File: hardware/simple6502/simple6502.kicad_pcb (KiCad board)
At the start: 2 copper layers, 87 x 85.6 mm, 24 parts, among them J1 ~{VP}, J2 CLK SEL, J6 AUX 5VDC, U1 W65C02SxP, U2 RAM 62256, U3 ROM 28C256, U4 74LS30, U5 74HCT00, U6 74HC138, X1 ACO-1MHz

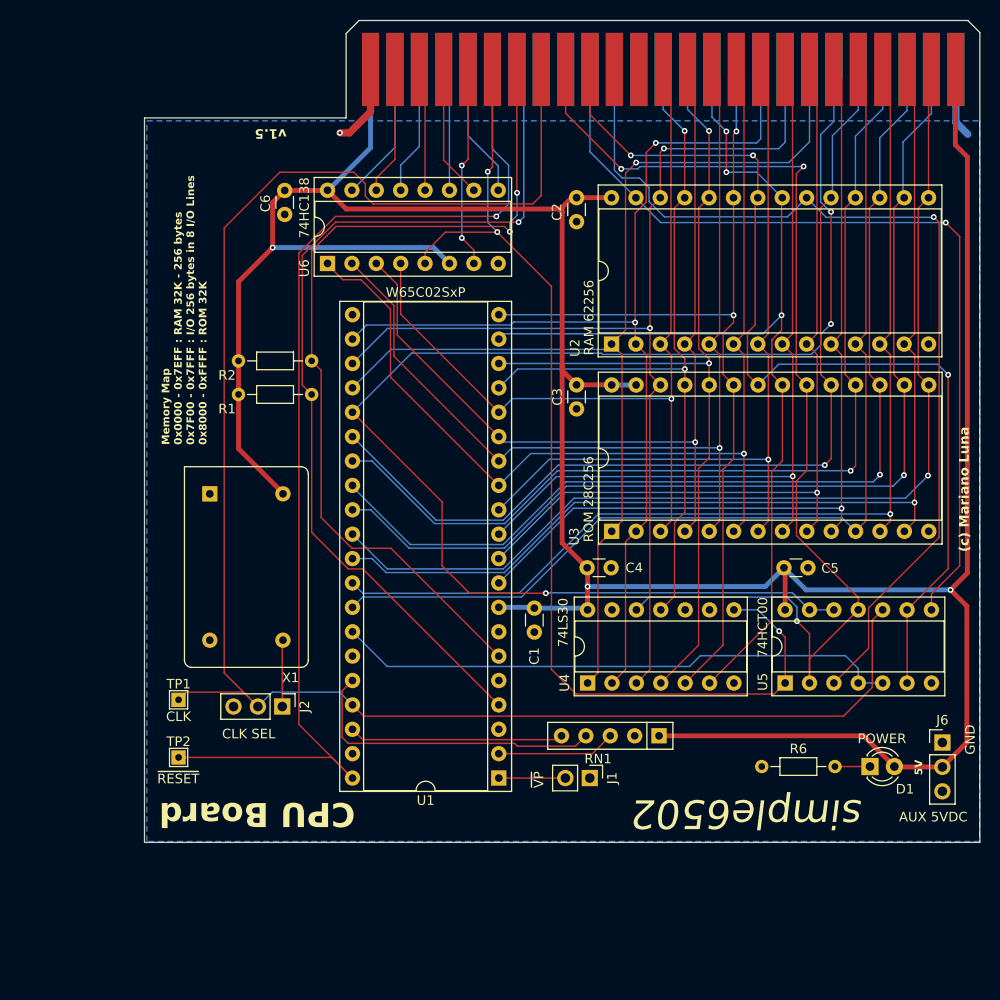
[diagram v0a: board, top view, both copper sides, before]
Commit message: Schematic and PCB cleanup
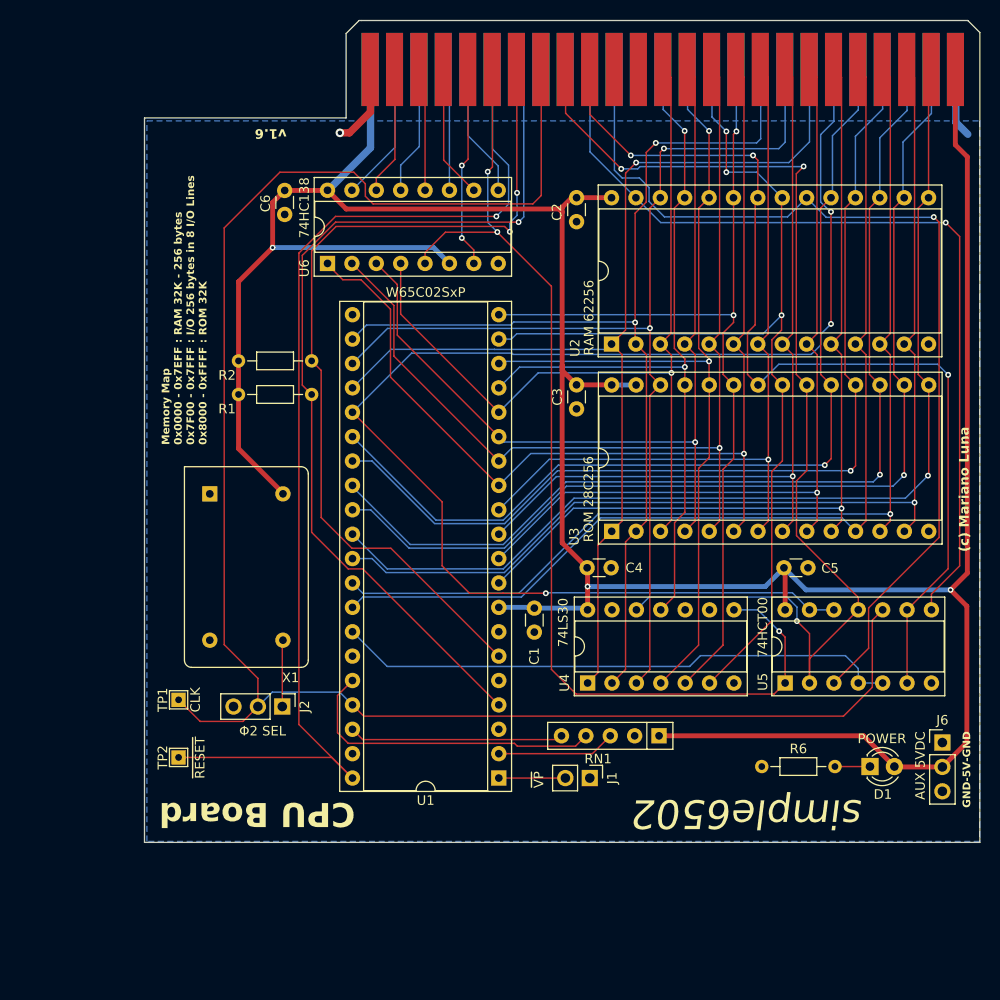
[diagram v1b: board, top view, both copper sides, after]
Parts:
- removed BUS1: 6502 BUS, Connector_PCBEdge:BUS_EdgePCB_Apple_2
- added SLOT1: 6502 BUS, Connector_PCBEdge:BUS_EdgePCB_Apple_2, F.Cu at (124.6, 55.1)
- J2: value CLK SEL -> Φ2 SEL
- turned TP1 to 90 degrees
- turned TP2 to 90 degrees
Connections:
- J2 pad 3: GND -> unconnected-(J2-Pin_3-Pad3)
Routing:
- net A7: track 88.2 -> 89.3 mm
- net CLK: track 187.0 -> 187.6 mm
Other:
- board text added: "GND-5V-GND"
- board text added: "Memory Map: 0x0000 - 0x7EFF : RAM 32K - 256 bytes 0x7F00 - 0x7FFF : I/O 256 bytes in 8 I/O Lines 0x8000 - 0xFFFF : ROM 32K"
- board text added: "v1.6"
- board text removed: "5V"
- board text removed: "GND"
- board text removed: "v1.5"

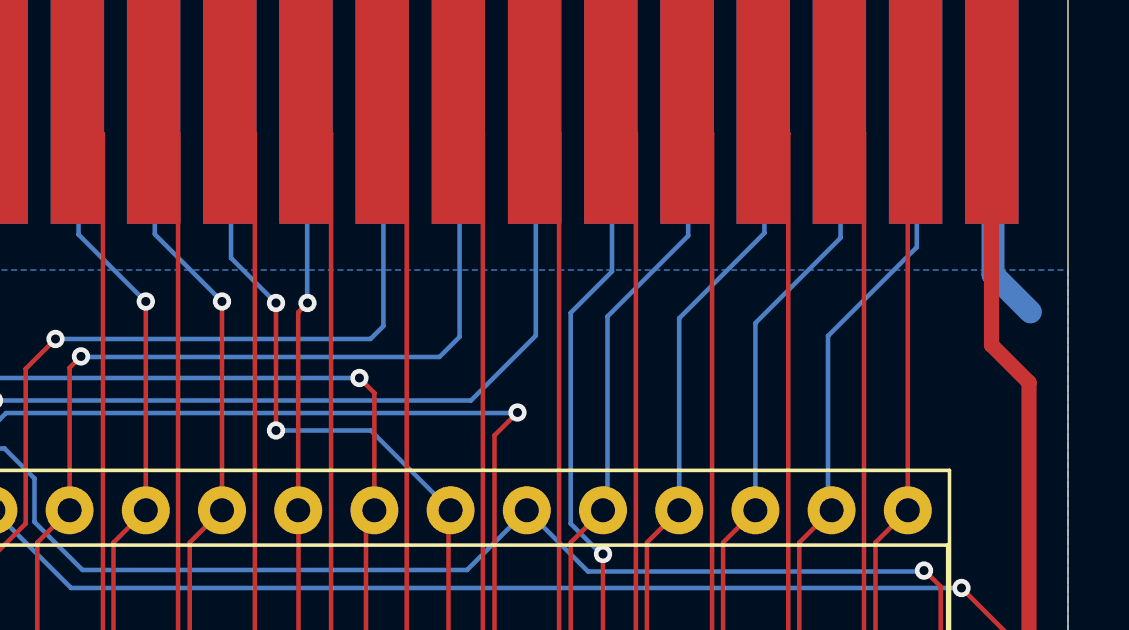
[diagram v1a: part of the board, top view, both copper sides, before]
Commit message: rev 1.8 new pcb optimized power routing
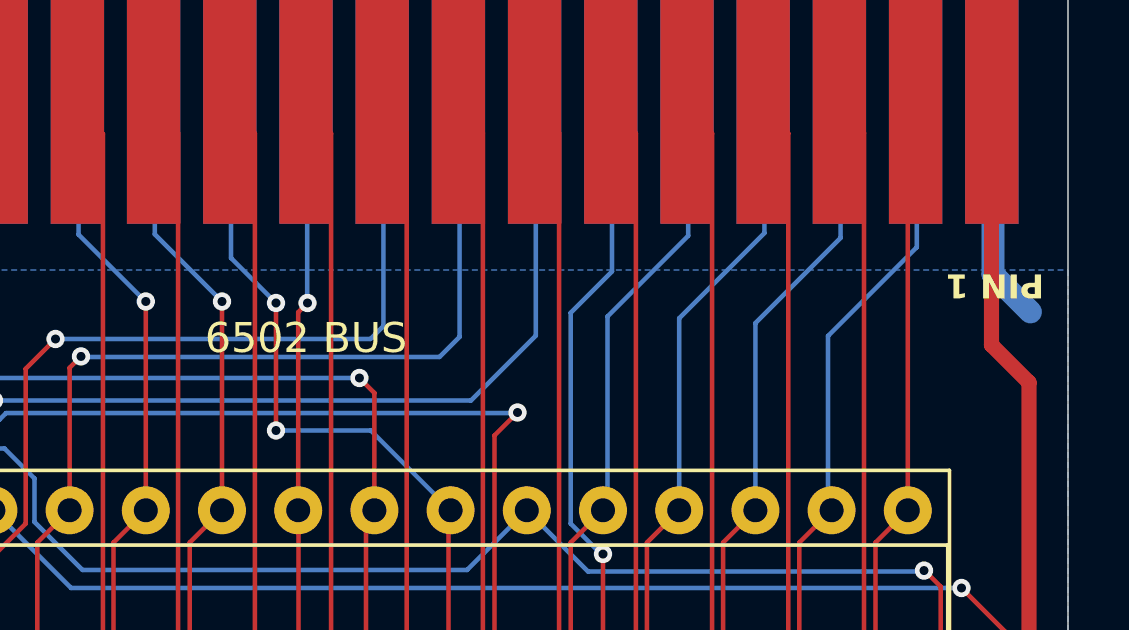
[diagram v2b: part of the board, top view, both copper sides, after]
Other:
- board text added: "PIN 1"
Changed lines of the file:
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@@
         (effects (font (size 1 1) (thickness 0.15)))
     )
-    (fp_text value "6502 BUS " (at 0 -7.62) (layer "F.Fab")
+    (fp_text value "6502 BUS " (at 0 -7.62 180) (layer "F.SilkS")
         (effects (font (size 1 1) (thickness 0.15)))
     )
@@
     (effects (font (size 1 1) (thickness 0.2) bold) (justify left bottom))
   )
+  (gr_text "PIN 1" (at 149.2 60.5 180) (layer "F.SilkS")
+    (effects (font (size 0.8 0.8) (thickness 0.15) bold) (justify left bottom))
+  )
   (gr_text "100x100mm PCBWay " (at 50 45) (layer "Cmts.User")

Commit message: Schematic rev 1.6 complete
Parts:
- moved J1 8.09 mm to (102.4, 133.0)
- moved X1 1.80 mm to (68.0, 99.2)
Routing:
- net /~{VP}: track 6.93 -> 4.12 mm
- net VCC: track 316.3 -> 315.5 mm
- net /OSC_OUT: track 6.94 -> 7.73 mm
- net A4: track 108.3 -> 107.6 mm

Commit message: cleanup and minor changes
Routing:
- net CLK: track 187.6 -> 175.4 mm
- net VCC: vias 3 -> 4
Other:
- board text added: "FRONT"
- board text added: "v${REVISION}"
- board text removed: "v1.6"

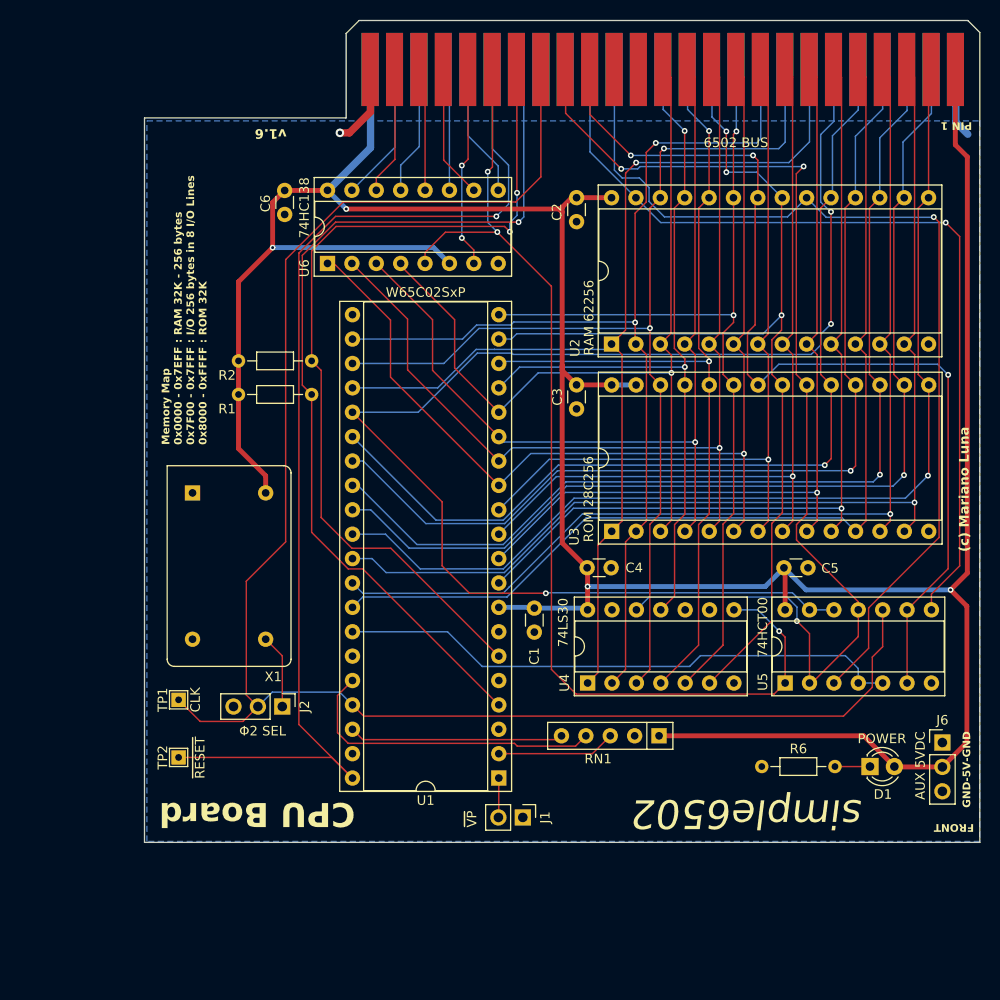
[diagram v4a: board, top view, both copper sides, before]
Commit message: Squashed commit of the following:
commit 7c3efda86e123a872d37b7a0967bfebff1f0e87c
Author: Mariano Luna <marianolu@gmail.com>
Date:   Wed Jun 26 21:29:25 2024 -0500

    added license to the read me

commit 04e24ff3751ecfd7aa1644195e6f678569023e69
Author: Mariano Luna <marianolu@gmail.com>
Date:   Wed Jun 26 21:19:54 2024 -0500

    typo fix for {\textunderscore}

commit 2b909ce419fda75b2b3b71af0dca9a0f271ced5f
Author: Mariano Luna <marianolu@gmail.com>
Date:   Wed Jun 26 21:10:17 2024 -0500

    updated ReadME and memory map in the schematic

commit 245ee8cf40a99742bf88408506d7aad409daa5ea
Author: Mariano Luna <marianolu@gmail.com>
Date:   Wed Jun 26 20:32:31 2024 -0500

    minor slikscreen additions

commit ba4f0f790206ee10e8f2da3f956f1fdfcce2d174
Author: Mariano Luna <marianolu@gmail.com>
Date:   Wed Jun 26 20:23:09 2024 -0500

    new PCB pics

commit 7135a14f7811bac113619ea70f1b15383090e088
Author: Mariano Luna <marianolu@gmail.com>
Date:   Wed Jun 26 20:16:23 2024 -0500

    minor silkscreen and trace tidy up

commit cb74d108b563011aa3ae8e77489211a7feb419d9
Author: Mariano Luna <marianolu@gmail.com>
Date:   Wed Jun 26 19:48:35 2024 -0500

    renumer components based on PCB placement

commit 755f9fae4396755bcef755a3da40c138a841726b
Author: Mariano Luna <marianolu@gmail.com>
Date:   Wed Jun 26 19:46:30 2024 -0500

    minor route changes

commit 2a8145687e928c766354ef12103bfb997fda5951
Author: Mariano Luna <marianolu@gmail.com>
Date:   Wed Jun 26 13:28:37 2024 -0500

    port wired, new slot pinout

commit 79f2ca33b26e56ed7b5b5aa909bf5c4120f9fd97
Author: Mariano Luna <marianolu@gmail.com>
Date:   Sat Jun 15 11:24:34 2024 -0500

    add the 40 pin header

commit 10816cce1296760c190b10fc9481db229a365134
Author: Mariano Luna <marianolu@gmail.com>
Date:   Tue Mar 26 20:31:24 2024 -0500

    Updated VCC routing

commit 6f1e481cf970100d714ca12a9d653bae0b6e1127
Author: Mariano Luna <marianolu@gmail.com>
Date:   Tue Mar 26 19:53:34 2024 -0500

    PCB ready DRC passed
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
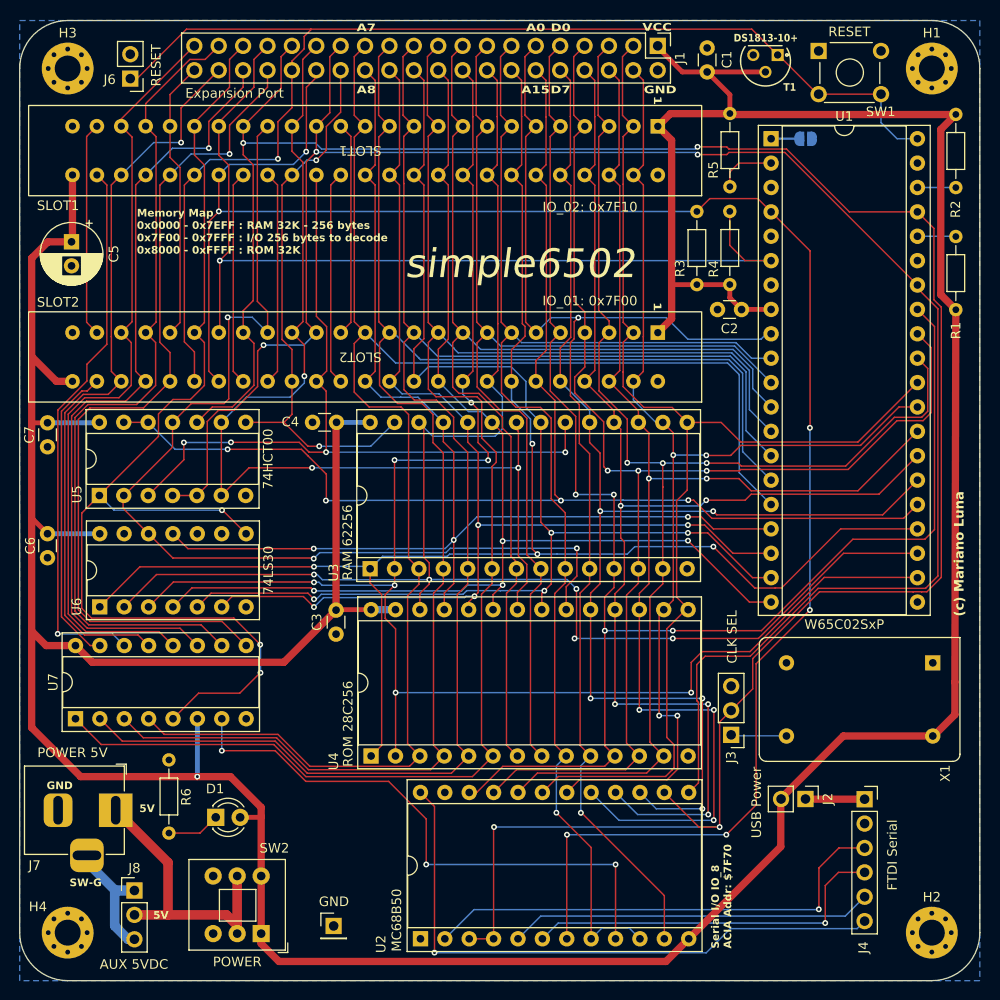
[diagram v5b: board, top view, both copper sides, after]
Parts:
- removed RN1: 4K7, Resistor_THT:R_Array_SIP5
- removed TP1: CLK, TestPoint:TestPoint_THTPad_1.5x1.5mm_Drill0.7mm
- removed TP2: ~{RESET}, TestPoint:TestPoint_THTPad_1.5x1.5mm_Drill0.7mm
- added C5: 1000uF, Capacitor_THT:CP_Radial_D6.3mm_P2.50mm, F.Cu at (55.4, 73.0)
- added H1: M, MountingHole:MountingHole_2.7mm_M2.5_Pad_Via, F.Cu at (145.0, 55.0)
- added H2: M, MountingHole:MountingHole_2.7mm_M2.5_Pad_Via, F.Cu at (145.0, 145.0)
- added H3: M, MountingHole:MountingHole_2.7mm_M2.5_Pad_Via, F.Cu at (55.0, 55.0)
- added H4: M, MountingHole:MountingHole_2.7mm_M2.5_Pad_Via, F.Cu at (55.0, 145.0)
- added J1: Expansion Port, Connector_PinHeader_2.54mm:PinHeader_2x20_P2.54mm_Vertical, F.Cu at (116.5, 52.6)
- added J2: USB Power, Connector_PinHeader_2.54mm:PinHeader_1x02_P2.54mm_Vertical, F.Cu at (131.8, 131.1)
- added J4: FTDI Serial, Connector_PinSocket_2.54mm:PinSocket_1x06_P2.54mm_Vertical, F.Cu at (138.0, 131.1)
- added J5: GND, Connector_PinHeader_2.54mm:PinHeader_1x01_P2.54mm_Vertical, F.Cu at (82.7, 144.3)
- added J6: RESET, Connector_PinHeader_2.54mm:PinHeader_1x02_P2.54mm_Vertical, F.Cu at (61.5, 56.0)
- added J7: POWER 5V, Connector_BarrelJack:BarrelJack_Horizontal, F.Cu at (60.0, 132.2)
- added R1: 4K7, Resistor_THT:R_Axial_DIN0204_L3.6mm_D1.6mm_P7.62mm_Horizontal, F.Cu at (147.5, 72.5)
- added R2: 4K7, Resistor_THT:R_Axial_DIN0204_L3.6mm_D1.6mm_P7.62mm_Horizontal, F.Cu at (147.5, 67.4)
- added R5: 4K7, Resistor_THT:R_Axial_DIN0204_L3.6mm_D1.6mm_P7.62mm_Horizontal, F.Cu at (124.0, 67.3)
- added SLOT2: IO_01: 0x7F00, Connector_Card:EDAC 395-050-520-201, F.Cu at (86.0, 85.0)
- added SW1: RESET, Button_Switch_THT:SW_TH_Tactile_Omron_B3F-10xx, F.Cu at (133.2, 53.2)
- added SW2: POWER, Button_Switch_THT:SW_Push_2P2T_Toggle_CK_PVA2OAH5xxxxxxV2, F.Cu at (75.2, 145.1)
- added T1: DS1813-10+, DS1813-10_:21-0248A, F.Cu at (126.4, 54.9)
- added U2: MC68B50, Package_DIP:DIP-24_W15.24mm_Socket, F.Cu at (91.7, 145.6)
- J3: renamed from J2; value Φ2 SEL -> CLK SEL
- J9: renamed from J1; footprint Connector_PinHeader_2.54mm:PinHeader_1x02_P2.54mm_Vertical -> Jumper:SolderJumper-2_P1.3mm_Open_RoundedPad1.0x1.5mm; moved to B.Cu
- R6: value 330 -> 220
- SLOT1: value 6502 BUS -> IO_02: 0x7F10; footprint Connector_PCBEdge:BUS_EdgePCB_Apple_2 -> Connector_Card:EDAC 395-050-520-201
- moved J8 85.5 mm to (62.0, 140.6)
- moved X1 79.1 mm to (145.1, 116.9), turned to 180 degrees
- moved C6 76.8 mm to (52.9, 103.5), turned to -90 degrees
- moved J9 76.6 mm to (131.9, 62.3), turned to 180 degrees
- moved U5 74.0 mm to (58.3, 99.5)
- moved U1 72.4 mm to (128.3, 62.3), turned to 0 degrees
- moved R6 69.7 mm to (65.5, 134.6), turned to 90 degrees
- moved D1 68.3 mm to (70.4, 133.0)
- moved C1 58.7 mm to (121.6, 55.4), turned to 90 degrees
- moved C7 58.2 mm to (52.9, 91.9), turned to -90 degrees
- moved U7 54.2 mm to (55.8, 122.7)
- moved U6 51.4 mm to (58.3, 111.1)
- moved C2 49.2 mm to (125.2, 80.1), turned to 180 degrees
- moved J3 46.8 mm to (124.1, 124.4), turned to 180 degrees
- moved R4 46.2 mm to (124.0, 69.9), turned to -90 degrees
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- renumbered C6 to C2, C2 to C4, C5 to C6, C4 to C7, J6 to J8, R1 to R3, R2 to R4, U2 to U3, U3 to U4, U4 to U6, U6 to U7
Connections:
- J3 pad 3: unconnected-(J2-Pin_3-Pad3) -> GND
- J8 pad 1: GND -> /Power and support/AUX GND
- J8 pad 2: VCC -> /Power and support/5VDC IN
- J8 pad 3: GND -> /Power and support/AUX GND
- SLOT1 pad 14: unconnected-(SLOT1-Pin_14-Pad14) -> GND
- SLOT1 pad 15: unconnected-(SLOT1-Pin_15-Pad15) -> R~{W}
- SLOT1 pad 21: ~{IO_08} -> BUS_21
- SLOT1 pad 24: ~{IO_02} -> BUS_24
- SLOT1 pad 27: ~{IO_01} -> ~{IO_02}
- SLOT1 pad 33: unconnected-(SLOT1-Pin_33-Pad33) -> BUS_33
- SLOT1 pad 34: unconnected-(SLOT1-Pin_34-Pad34) -> BUS_34
- SLOT1 pad 37: unconnected-(SLOT1-Pin_37-Pad37) -> GND
- U1 pad 2: RDY -> /RDY
- U1 pad 36: BE -> /BE
- U1 pad 38: ~{SO} -> /~{SO}
- U6 pad 2: A12 -> A13
- U6 pad 3: A13 -> A12
- U6 pad 4: A9 -> A11
- U6 pad 5: A11 -> A10
- U6 pad 6: A10 -> A9
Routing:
- net R~{W}: track 59.2 -> 202.3 mm, vias 0 -> 3
- net VCC: track 315.5 -> 430.8 mm, vias 4 -> 1
- net ~{IRQ}: track 96.6 -> 197.6 mm, vias 1 -> 6
- net A7: track 89.3 -> 168.5 mm, vias 1 -> 0
- net ~{IO_07}: track 13.9 -> 89.9 mm, vias 0 -> 1
- net A6: track 93.8 -> 168.4 mm, vias 1 -> 0
- net ~{IO_06}: track 13.9 -> 87.5 mm
- net ~{IO_05}: track 12.8 -> 83.9 mm, vias 0 -> 1
- net CLK: track 175.4 -> 245.9 mm, vias 0 -> 4
- net A5: track 100.3 -> 168.9 mm, vias 1 -> 0
- net ~{IO_04}: track 12.8 -> 80.8 mm
- net A12: track 107.6 -> 172.9 mm, vias 2 -> 7
- net ~{IO_03}: track 13.4 -> 77.5 mm, vias 0 -> 1
- net ~{CTS}: track 0.00 -> 63.5 mm, vias 0 -> 1
- net A4: track 107.6 -> 171.0 mm, vias 1 -> 0
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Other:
- board size 87 x 85.6 mm -> 100 x 100 mm
- board text added: "5V"
- board text added: "A0"
- board text added: "A15"
- board text added: "A7"
- board text added: "A8"
- board text added: "D0"
- board text added: "D7"
- board text added: "GND"
- board text added: "Memory Map 0x0000 - 0x7EFF : RAM 32K - 256 bytes 0x7F00 - 0x7FFF : I/O 256 bytes to decode 0x8000 - 0xFFFF : ROM 32K"
- board text added: "SW-G"
- board text added: "Serial I/O IO_8 ACIA Addr: $7F70"
- board text added: "VCC"
- board text added: "~{RESET}"
- board text removed: "CPU Board"
- board text removed: "FRONT"
- board text removed: "GND-5V-GND"
- board text removed: "Memory Map 0x0000 - 0x7EFF : RAM 32K - 256 bytes 0x7F00 - 0x7FFF : I/O 256 bytes in 8 I/O Lines 0x8000 - 0xFFFF : ROM 32K"
- board text removed: "Memory Map Address Space 0x0000 - 0x7EFF : RAM 32K - 256 bytes 0x7F00 - 0x7FFF : I/O 256 bytes decoded in 8 IO Lines 0x8000 - 0xFFFF : ROM 32K"
- board text removed: "Memory Map: 0x0000 - 0x7EFF : RAM 32K - 256 bytes 0x7F00 - 0x7FFF : I/O 256 bytes in 8 I/O Lines 0x8000 - 0xFFFF : ROM 32K"
- board text removed: "PIN 1"
- board text removed: "v${REVISION}"

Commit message: Rev 1.5 complete
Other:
- board text added: "Rev: ${REVISION}"
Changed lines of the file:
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@@
   )
   (paper "A4")
+  (title_block
+    (title "Simple 6502 - All in One")
+    (date "2024-06-26")
+    (rev "1.5")
+  )
   (layers
     (0 "F.Cu" signal)
@@
     (effects (font (size 0.8 1) (thickness 0.15) bold) (justify left bottom))
   )
+  (gr_text "Rev: ${REVISION}" (at 148.75 139.64 90) (layer "F.SilkS")
+    (effects (font (size 1 1) (thickness 0.2) bold) (justify left bottom))
+  )
   (gr_text "D7" (at 105.28 57.68) (layer "F.SilkS")

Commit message: Version 1.6 Final
Added solder pads just in case
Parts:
- added JP1: RAM_~{OE}, Jumper:SolderJumper-2_P1.3mm_Bridged_RoundedPad1.0x1.5mm, F.Cu at (101.7, 95.9)
- added JP2: ~{WR}, Jumper:SolderJumper-2_P1.3mm_Bridged_RoundedPad1.0x1.5mm, B.Cu at (87.7, 94.1)
- added JP3: ROM_~{OE}, Jumper:SolderJumper-2_P1.3mm_Bridged_RoundedPad1.0x1.5mm, F.Cu at (101.7, 100.4)
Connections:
- U3 pad 22: ~{RD} -> /RAM_~{OE}
- U3 pad 27: ~{WR} -> /RAM_~{WE}
- U4 pad 22: ~{RD} -> /ROM_~{OE}
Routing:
- net ~{RD}: track 108.1 -> 92.2 mm
- net /ROM_~{OE}: track 0.00 -> 11.2 mm
- net /RAM_~{OE}: track 0.00 -> 3.45 mm
- net A15: track 136.8 -> 139.7 mm
- net ~{WR}: track 58.1 -> 55.3 mm
- net /RAM_~{WE}: track 0.00 -> 2.55 mm
- net TXD: track 38.7 -> 40.5 mm, vias 1 -> 0
- net CLK: track 245.9 -> 246.9 mm
- net ~{RAM_CS}: track 80.5 -> 81.1 mm, vias 4 -> 3
- net A12: track 172.9 -> 172.4 mm
- net RXD: track 50.2 -> 50.0 mm, vias 1 -> 0
